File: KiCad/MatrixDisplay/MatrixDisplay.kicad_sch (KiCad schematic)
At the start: 3 parts, among them J1 PUT_IN, J2 Power, U1 mini_esp32

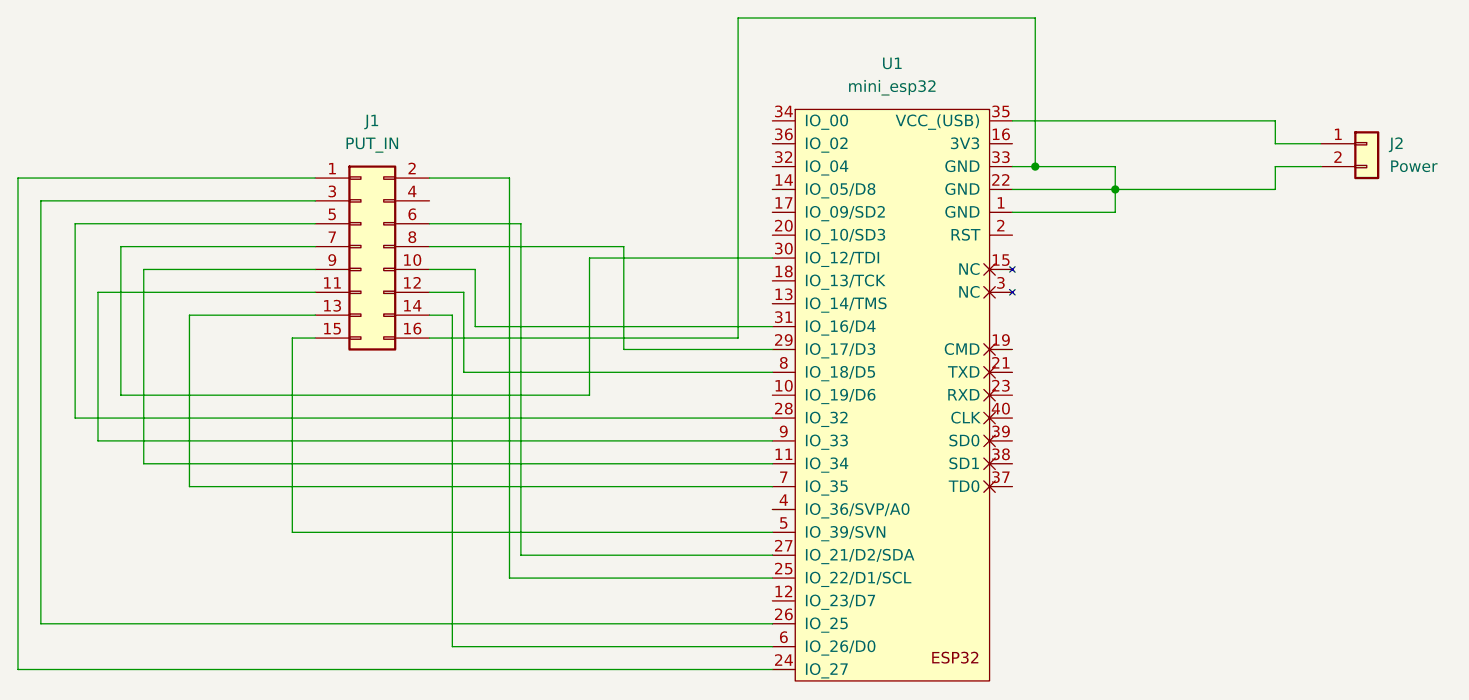
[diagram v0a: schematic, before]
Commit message: updated pinout used for PCB Adapter
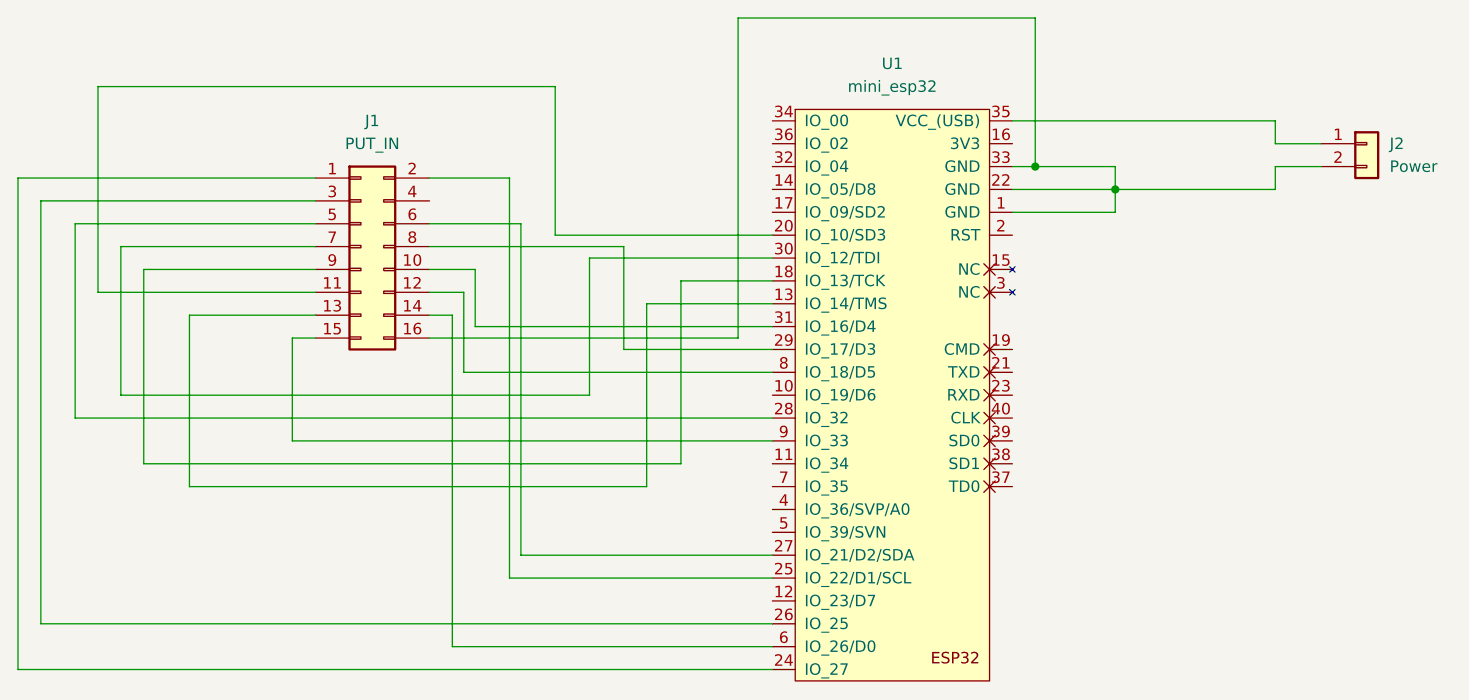
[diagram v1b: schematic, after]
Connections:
- net at U1.11 (IO_34): no longer J1.9 (Pin_9)
- net at U1.13 (IO_14/TMS): now also J1.13 (Pin_13)
- net at U1.18 (IO_13/TCK): now also J1.9 (Pin_9)
- net at U1.20 (IO_10/SD3): now also J1.11 (Pin_11)
- net at U1.5 (IO_39/SVN): no longer J1.15 (Pin_15)
- net at U1.7 (IO_35): no longer J1.13 (Pin_13)
- net at U1.9 (IO_33): now also J1.15 (Pin_15); no longer J1.11 (Pin_11)
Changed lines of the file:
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@@
+    (stroke (width 0) (type default) (color 0 0 0 0))
+  )
+  (wire (pts (xy 60.96 74.93) (xy 60.96 52.07))
     (stroke (width 0) (type default) (color 0 0 0 0))
   )
   (wire (pts (xy 106.68 106.68) (xy 106.68 62.23))
+    (stroke (width 0) (type default) (color 0 0 0 0))
+  )
+  (wire (pts (xy 82.55 91.44) (xy 135.89 91.44))
     (stroke (width 0) (type default) (color 0 0 0 0))
   )
@@
     (stroke (width 0) (type default) (color 0 0 0 0))
   )
-  (wire (pts (xy 135.89 96.52) (xy 71.12 96.52))
+  (wire (pts (xy 125.73 73.66) (xy 135.89 73.66))
     (stroke (width 0) (type default) (color 0 0 0 0))
   )
@@
     (stroke (width 0) (type default) (color 0 0 0 0))
   )
+  (wire (pts (xy 111.76 52.07) (xy 111.76 68.58))
+    (stroke (width 0) (type default) (color 0 0 0 0))
+  )
   (wire (pts (xy 63.5 69.85) (xy 85.09 69.85))
     (stroke (width 0) (type default) (color 0 0 0 0))
@@
   )
   (wire (pts (xy 135.89 83.82) (xy 101.6 83.82))
+    (stroke (width 0) (type default) (color 0 0 0 0))
+  )
+  (wire (pts (xy 125.73 93.98) (xy 125.73 73.66))
     (stroke (width 0) (type default) (color 0 0 0 0))
   )
@@
   )
   (wire (pts (xy 66.04 72.39) (xy 85.09 72.39))
+    (stroke (width 0) (type default) (color 0 0 0 0))
+  )
+  (wire (pts (xy 71.12 96.52) (xy 121.92 96.52))
     (stroke (width 0) (type default) (color 0 0 0 0))
   )
@@
     (stroke (width 0) (type default) (color 0 0 0 0))
   )
-  (wire (pts (xy 60.96 74.93) (xy 60.96 91.44))
-    (stroke (width 0) (type default) (color 0 0 0 0))
-  )
   (wire (pts (xy 191.77 58.42) (xy 191.77 55.88))
     (stroke (width 0) (type default) (color 0 0 0 0))
   )
   (wire (pts (xy 71.12 77.47) (xy 85.09 77.47))
+    (stroke (width 0) (type default) (color 0 0 0 0))
+  )
+  (wire (pts (xy 66.04 93.98) (xy 125.73 93.98))
     (stroke (width 0) (type default) (color 0 0 0 0))
   )
@@
     (stroke (width 0) (type default) (color 0 0 0 0))
   )
-  (wire (pts (xy 82.55 101.6) (xy 82.55 80.01))
-    (stroke (width 0) (type default) (color 0 0 0 0))
-  )
-  (wire (pts (xy 135.89 91.44) (xy 60.96 91.44))
-    (stroke (width 0) (type default) (color 0 0 0 0))
-  )
   (wire (pts (xy 191.77 55.88) (xy 162.56 55.88))
     (stroke (width 0) (type default) (color 0 0 0 0))
@@
   )
   (wire (pts (xy 63.5 86.36) (xy 63.5 69.85))
+    (stroke (width 0) (type default) (color 0 0 0 0))
+  )
+  (wire (pts (xy 121.92 76.2) (xy 135.89 76.2))
     (stroke (width 0) (type default) (color 0 0 0 0))
   )
@@
     (stroke (width 0) (type default) (color 0 0 0 0))
   )
-  (wire (pts (xy 135.89 101.6) (xy 82.55 101.6))
-    (stroke (width 0) (type default) (color 0 0 0 0))
-  )
   (wire (pts (xy 66.04 72.39) (xy 66.04 93.98))
     (stroke (width 0) (type default) (color 0 0 0 0))
@@
     (stroke (width 0) (type default) (color 0 0 0 0))
   )
-  (wire (pts (xy 100.33 114.3) (xy 100.33 77.47))
+  (wire (pts (xy 82.55 80.01) (xy 82.55 91.44))
     (stroke (width 0) (type default) (color 0 0 0 0))
   )
-  (wire (pts (xy 135.89 93.98) (xy 66.04 93.98))
+  (wire (pts (xy 121.92 96.52) (xy 121.92 76.2))
+    (stroke (width 0) (type default) (color 0 0 0 0))
+  )
+  (wire (pts (xy 60.96 52.07) (xy 111.76 52.07))
+    (stroke (width 0) (type default) (color 0 0 0 0))
+  )
+  (wire (pts (xy 100.33 114.3) (xy 100.33 77.47))
     (stroke (width 0) (type default) (color 0 0 0 0))
   )
@@
     (stroke (width 0) (type default) (color 0 0 0 0))
   )
+  (wire (pts (xy 111.76 68.58) (xy 135.89 68.58))
+    (stroke (width 0) (type default) (color 0 0 0 0))
+  )
